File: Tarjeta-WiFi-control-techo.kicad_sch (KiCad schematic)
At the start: 80 parts, among them J2 Conn_ARM_SWD_TagConnect_TC203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, J3 Conn_01x04_Pin, J4 Conn_01x02_Pin, J6 Conn_01x03_Socket, J7 Conn_01x09_Socket, Q2 BC817-40, Q3 BSS84P, SW1 SW_Push, U1 ESP32-WROOM-32E, U3 BH1750FVI-TR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

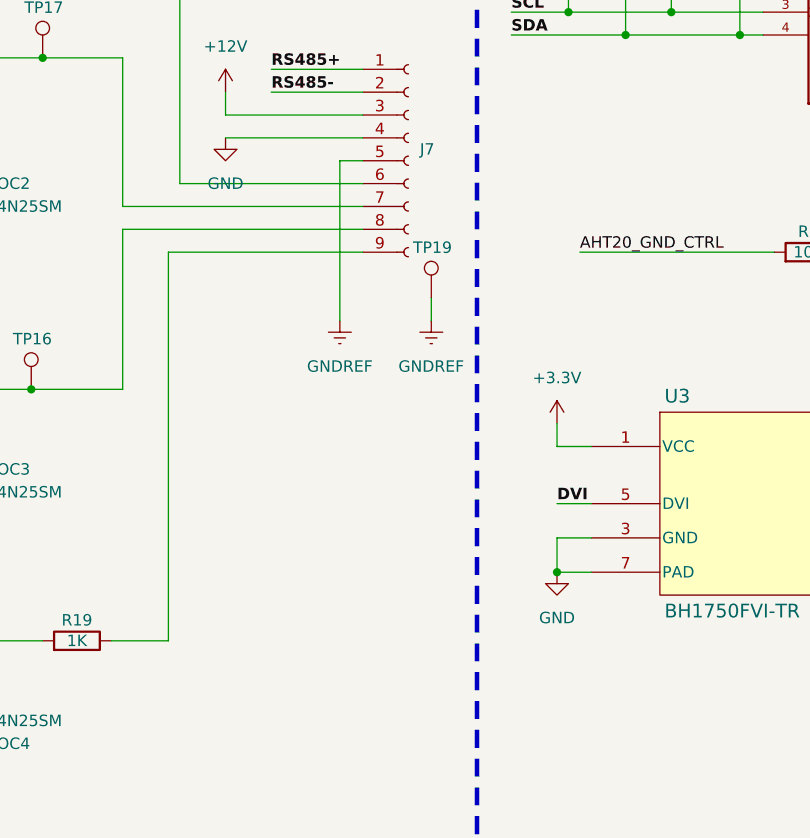
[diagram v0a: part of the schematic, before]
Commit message: Se agrego un conector para poder hacer uso del control manual
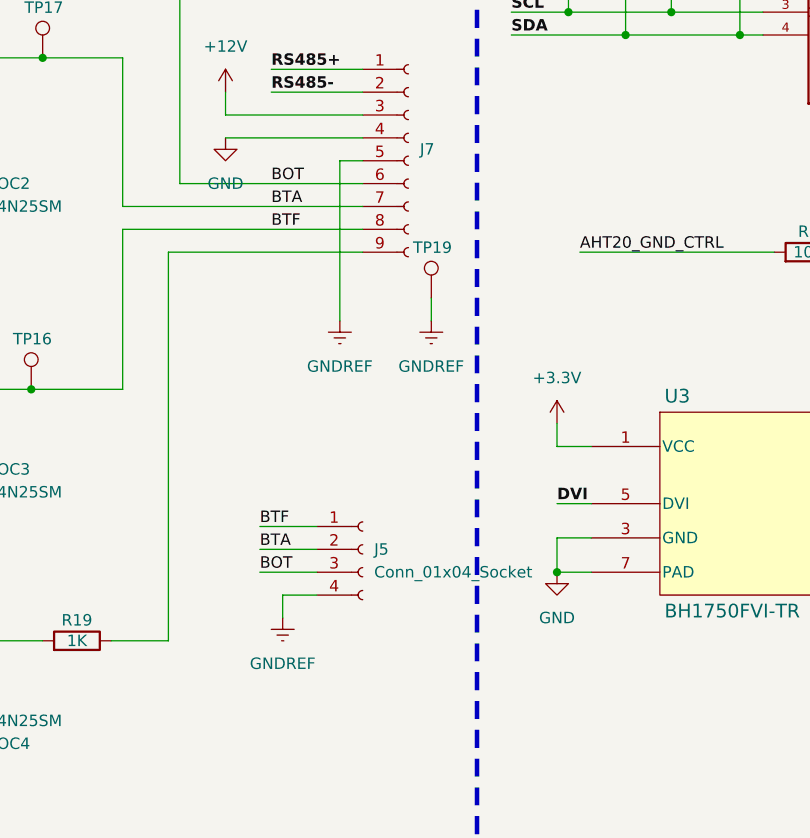
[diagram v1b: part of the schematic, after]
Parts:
- added J5: Conn_01x04_Socket, Connector_Phoenix_MC:PhoenixContact_MC_1,5_4-G-3.81_1x04_P3.81mm_Horizontal, symbol Connector:Conn_01x04_Socket
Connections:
- net GNDREF: now also J5.4 (Pin_4)
- net BOT: now reaches J7.6 (Pin_6), OC1.5, TP18.1
- net BOT: now also J5.3 (Pin_3)
- net BTA: now reaches J7.7 (Pin_7), OC2.5, TP17.1
- net BTA: now also J5.2 (Pin_2)
- net BTF: now reaches J7.8 (Pin_8), OC3.5, TP16.1
- net BTF: now also J5.1 (Pin_1)
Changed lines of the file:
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@@
 		)
 	)
+	(wire
+		(pts
+			(xy 266.7 125.73) (xy 266.7 128.27)
+		)
+		(stroke
+			(width 0)
+			(type default)
+		)
+	)
 	(polyline
 		(pts
@@
 	(wire
 		(pts
+			(xy 270.51 125.73) (xy 266.7 125.73)
+		)
+		(stroke
+			(width 0)
+			(type default)
+		)
+	)
+	(wire
+		(pts
 			(xy 41.91 132.08) (xy 59.69 132.08)
 		)
@@
 	(wire
 		(pts
+			(xy 264.16 120.65) (xy 270.51 120.65)
+		)
+		(stroke
+			(width 0)
+			(type default)
+		)
+	)
+	(wire
+		(pts
 			(xy 231.14 107.95) (xy 231.14 102.87)
 		)
@@
 	(wire
 		(pts
+			(xy 264.16 118.11) (xy 270.51 118.11)
+		)
+		(stroke
+			(width 0)
+			(type default)
+		)
+	)
+	(wire
+		(pts
 			(xy 60.96 224.79) (xy 60.96 227.33)
 		)
@@
 	(wire
 		(pts
+			(xy 264.16 123.19) (xy 270.51 123.19)
+		)
+		(stroke
+			(width 0)
+			(type default)
+		)
+	)
+	(wire
+		(pts
 			(xy 273.05 77.47) (xy 273.05 95.25)
 		)
@@
 		)
 	)
+	(label "BTF"
+		(at 265.43 85.09 0)
+		(effects
+			(font
+				(size 1.27 1.27)
+			)
+			(justify left bottom)
+		)
+	)
+	(label "BTA"
+		(at 265.43 82.55 0)
+		(effects
+			(font
+				(size 1.27 1.27)
+			)
+			(justify left bottom)
+		)
+	)
 	(label "RS485+"
 		(at 93.98 201.93 180)
@@
 		)
 	)
+	(label "BOT"
+		(at 264.16 123.19 0)
+		(effects
+			(font
+				(size 1.27 1.27)
+			)
+			(justify left bottom)
+		)
+	)
 	(label "RS485+"
 		(at 265.43 67.31 0)
@@
 		)
 	)
+	(label "BOT"
+		(at 265.43 80.01 0)
+		(effects
+			(font
+				(size 1.27 1.27)
+			)
+			(justify left bottom)
+		)
+	)
 	(label "N_FIL"
 		(at 267.97 191.77 0)
@@
 		)
 	)
+	(label "BTF"
+		(at 264.16 118.11 0)
+		(effects
+			(font
+				(size 1.27 1.27)
+			)
+			(justify left bottom)
+		)
+	)
 	(label "RXDO"
 		(at 113.03 62.23 180)
@@
 		)
 	)
+	(label "BTA"
+		(at 264.16 120.65 0)
+		(effects
+			(font
+				(size 1.27 1.27)
+			)
+			(justify left bottom)
+		)
+	)
 	(label "BTF_M"
 		(at 185.42 105.41 0)
@@
 	)
 	(symbol
+		(lib_id "power:GNDREF")
+		(at 266.7 128.27 0)
+		(unit 1)
+		(exclude_from_sim no)
+		(in_bom yes)
+		(on_board yes)
+		(dnp no)
+		(fields_autoplaced yes)
+		(property "Reference" "#PWR057"
+			(at 266.7 134.62 0)
+			(effects
+				(font
+					(size 1.27 1.27)
+				)
+				(hide yes)
+			)
+		)
+		(property "Value" "GNDREF"
+			(at 266.7 133.35 0)
+			(effects
+				(font
+					(size 1.27 1.27)
+				)
+			)
+		)
+		(property "Footprint" ""
+			(at 266.7 128.27 0)
+			(effects
+				(font
+					(size 1.27 1.27)
+				)
+				(hide yes)
+			)
+		)
+		(property "Datasheet" ""
+			(at 266.7 128.27 0)
+			(effects
+				(font
+					(size 1.27 1.27)
+				)
+				(hide yes)
+			)
+		)
+		(property "Description" "Power symbol creates a global label with name \"GNDREF\" , reference supply ground"
+			(at 266.7 128.27 0)
+			(effects
+				(font
+					(size 1.27 1.27)
+				)
+				(hide yes)
+			)
+		)
+		(pin "1"
+		)
+		(instances
+			(project "Tarjeta-WiFi-control-techo"
+				(path "/3b137950-8037-4a70-834a-586849b3917d"
+					(reference "#PWR057")
+					(unit 1)
+				)
+			)
+		)
+	)
+	(symbol
 		(lib_id "PCM_Capacitor_AKL:C_0805")
 		(at 127 35.56 0)
@@
 					(unit 1)
 				)
+			)
+		)
+	)
+	(symbol
+		(lib_id "Connector:Conn_01x04_Socket")
+		(at 275.59 120.65 0)
+		(unit 1)
+		(exclude_from_sim no)
+		(in_bom yes)
+		(on_board yes)
+		(dnp no)
+		(fields_autoplaced yes)
+		(property "Reference" "J5"
+			(at 276.86 120.6499 0)
+			(effects
+				(font
+					(size 1.27 1.27)
+				)
+				(justify left)
+			)
+		)
+		(property "Value" "Conn_01x04_Socket"
+			(at 276.86 123.1899 0)
+			(effects
+				(font
+					(size 1.27 1.27)
+				)
+				(justify left)
+			)
+		)
+		(property "Footprint" "Connector_Phoenix_MC:PhoenixContact_MC_1,5_4-G-3.81_1x04_P3.81mm_Horizontal"
+			(at 275.59 120.65 0)
+			(effects
+				(font
+					(size 1.27 1.27)
+				)
+				(hide yes)
+			)
+		)
+		(property "Datasheet" "~"
+			(at 275.59 120.65 0)
+			(effects
+				(font
+					(size 1.27 1.27)
+				)
+				(hide yes)
+			)
+		)
+		(property "Description" "Generic connector, single row, 01x04, script generated"
+			(at 275.59 120.65 0)
+			(effects
+				(font
+					(size 1.27 1.27)
+				)
+				(hide yes)
+			)
+		)
+		(pin "4"
+		)
+		(pin "2"
+		)
+		(pin "1"
+		)
+		(pin "3"
+		)
+		(instances
+			(project ""
+				(path "/3b137950-8037-4a70-834a-586849b3917d"
+					(reference "J5")
+					(unit 1)
+				)

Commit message: final release
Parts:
- J5: MANUFACTURER (none) -> Phoenix Contact; MPN (none) -> 1803293
- J7: MANUFACTURER (none) -> Phoenix Contact; MPN (none) -> 1803345
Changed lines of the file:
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@@
+			)
+		)
+		(property "MPN" "1803293 "
+			(at 275.59 120.65 0)
+			(effects
+				(font
+					(size 1.27 1.27)
+				)
+				(hide yes)
+			)
+		)
+		(property "MANUFACTURER" "Phoenix Contact"
+			(at 275.59 120.65 0)
+			(effects
+				(font
+					(size 1.27 1.27)
+				)
+				(hide yes)
+			)
+		)
+		(property "Link" ""
+			(at 275.59 120.65 0)
+			(effects
+				(font
+					(size 1.27 1.27)
+				)
+				(hide yes)
+			)
+		)
+		(property "Price" ""
+			(at 275.59 120.65 0)
+			(effects
+				(font
+					(size 1.27 1.27)
+				)
+				(hide yes)
 			)
 		)
@@
 			)
 		)
-		(property "MPN" ""
+		(property "MPN" "1803345 "
 			(at 280.67 77.47 0)
 			(effects
@@
 			)
 		)
-		(property "MANUFACTURER" ""
+		(property "MANUFACTURER" "Phoenix Contact"
 			(at 280.67 77.47 0)
 			(effects
